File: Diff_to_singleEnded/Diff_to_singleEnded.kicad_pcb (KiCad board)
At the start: 4 copper layers, 85 x 65 mm, 45 parts, among them IC1 ULN2003LVDR, J1 1725672, J2 1725672, J3 1725672, J4 1725672, J5 1725672, J6 1725672, J7 1725672, K3 EE2-5NU, U1 OPA1692xD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

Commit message: removed Relay and power supples related items from board and add seperate ground plains for signal and power
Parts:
- removed C11: 100n, Capacitor_SMD:C_0805_2012Metric_Pad1.18x1.45mm_HandSolder
- removed IC1: ULN2003LVDR, samsys:SOIC127P780X200-16N
- removed J2, J6, J7: 1725672, samsys:1725672
- removed K3: EE2-5NU, samsys:EE2-5NU
- moved J3 13.7 mm to (176.0, 82.3)
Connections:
- C1 pad 2: /Left in -> /Lout
- C13 pad 1: GND -> GND 2
- C14 pad 1: GND -> GND 2
- C15 pad 1: GND -> GND 2
- C2 pad 2: /right in -> /Rout
- J3 pad 1: /right out -> /Lout
- J3 pad 2: GND -> GND 2
- J3 pad 3: GND -> GND 2
- J3 pad 4: /Left Out -> /Rout
- J4 pad 2: GND -> GND 2
- J4 pad 3: GND -> GND 2
- J5 pad 2: GND -> GND 2
- J5 pad 3: GND -> GND 2
- R10 pad 2: /right in -> /Rout
- R5 pad 2: GND -> GND 2
- R6 pad 1: GND -> GND 2
- R8 pad 1: GND -> GND 2
- R9 pad 2: /Left in -> /Lout
- U3 pad 1: /Left in -> /Lout
- U3 pad 7: /right in -> /Rout
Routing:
- net /Lout: track 0.00 -> 47.5 mm, vias 0 -> 1
- net /Rout: track 0.00 -> 42.3 mm, vias 0 -> 1
- net +5VP: track 41.6 -> 0.00 mm, vias 1 -> 0
- net /right in: track 37.9 -> 0.00 mm, vias 1 -> 0
- net /Relay Out: track 34.8 -> 0.00 mm, vias 2 -> 0
- net /Left in: track 33.9 -> 0.00 mm, vias 1 -> 0
- net /right out: track 29.3 -> 0.00 mm
- net /Left Out: track 23.6 -> 0.00 mm
- net /left in ext: track 18.4 -> 0.00 mm
- net /relay 1 in: track 16.4 -> 0.00 mm
- net /right in ext: track 8.18 -> 0.00 mm
- net GND 2: track 0.00 -> 6.68 mm, vias 0 -> 3
- net GND: track 8.83 -> 2.15 mm, vias 137 -> 134
- removed copper zone on B.Cu, net GND
- removed copper zone on F.Cu, net GND
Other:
- board text removed: "5v Relay G"
- board text removed: "G"
- board text removed: "Output"
- board text removed: "Relay"
- board text removed: "Sig"

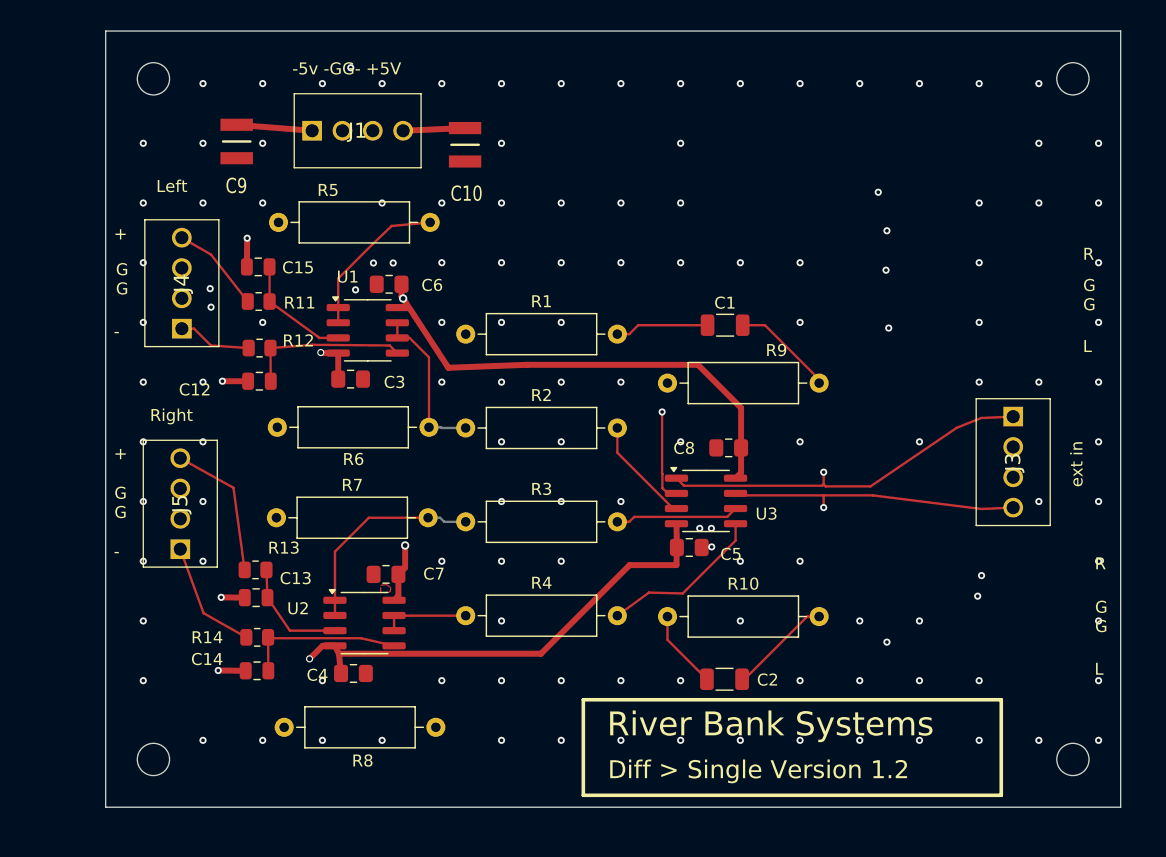
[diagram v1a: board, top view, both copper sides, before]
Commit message: added new rpi power board
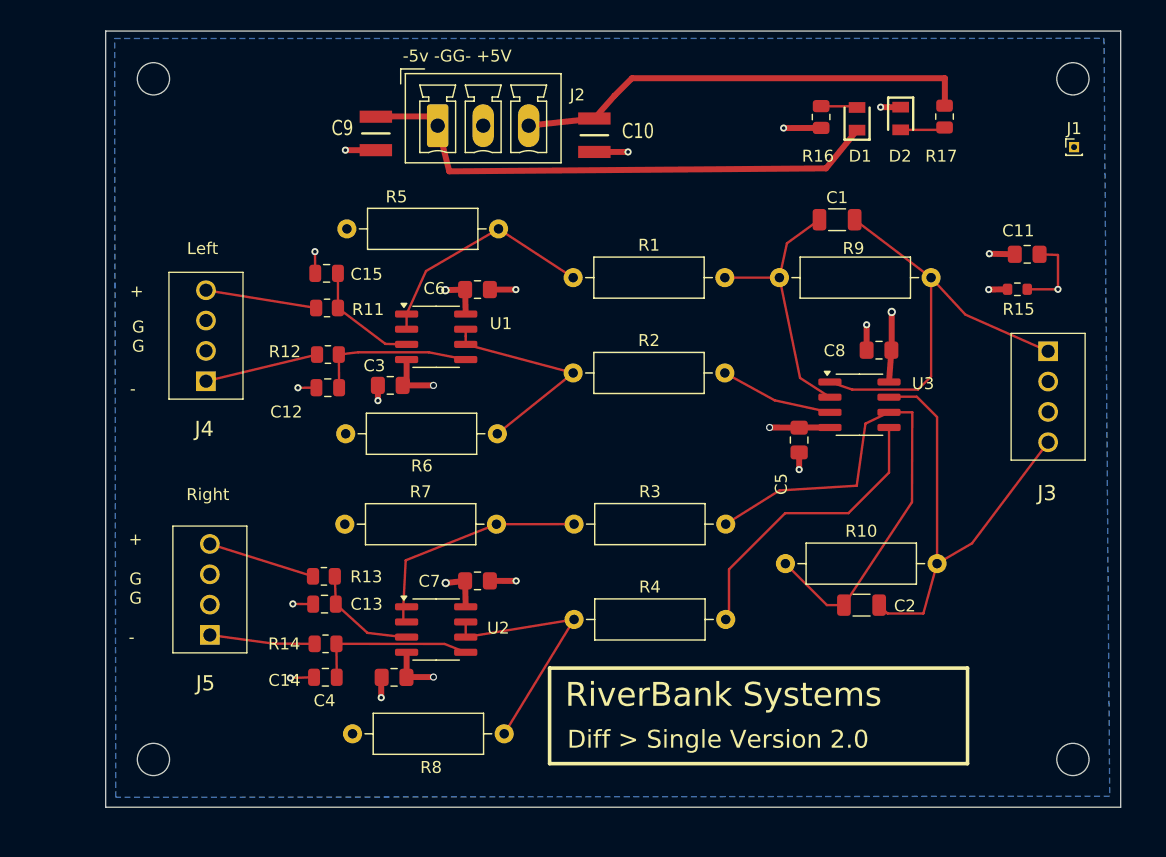
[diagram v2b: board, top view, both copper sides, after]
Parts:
- added C11: 100n, Capacitor_SMD:C_0805_2012Metric_Pad1.18x1.45mm_HandSolder, F.Cu at (177.2, 68.7)
- added D1: LED, samsys:LEDC2012X40N, F.Cu at (162.9, 57.4)
- added D2: LED, samsys:LEDC2012X40N, F.Cu at (166.6, 57.3)
- added J2: Conn_01x03_Socket, Connector_Phoenix_MC:PhoenixContact_MCV_1,5_3-G-3.81_1x03_P3.81mm_Vertical, F.Cu at (127.8, 57.9)
- added R15: 10, Resistor_SMD:R_0603_1608Metric, F.Cu at (176.3, 71.6)
- added R16: 1k, Resistor_SMD:R_0805_2012Metric, F.Cu at (159.9, 57.2)
- added R17: 1k, Resistor_SMD:R_0805_2012Metric, F.Cu at (170.2, 57.2)
- J1: value 1725672 -> Conn_01x01_Pin; footprint samsys:1725672 -> Connector_PinHeader_1.00mm:PinHeader_1x01_P1.00mm_Vertical
- moved J1 63.8 mm to (181.1, 59.7)
- moved U3 15.2 mm to (163.1, 81.3)
- moved C8 15.0 mm to (164.8, 76.7)
- moved C2 13.0 mm to (163.3, 98.1)
- moved C1 12.9 mm to (161.2, 65.8)
- moved R9 12.9 mm to (156.4, 70.7)
- moved C5 12.9 mm to (158.1, 84.2), turned to -90 degrees
- moved C9 11.7 mm to (122.6, 58.6)
- moved C10 10.9 mm to (140.9, 58.7)
- moved R10 10.8 mm to (156.9, 94.6)
- moved R1 10.2 mm to (139.2, 70.7)
- moved R2 10.1 mm to (139.2, 78.6)
- moved R4 9.08 mm to (139.2, 99.3)
- moved R3 9.08 mm to (139.2, 91.3)
- moved C7 7.68 mm to (131.1, 96.0), turned to 180 degrees
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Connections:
- C12 pad 1: GND -> GND 2
- J1 pad 1: -5V -> GND 3
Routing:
- net +5V: track 87.0 -> 160.3 mm, vias 2 -> 3
- net -5V: track 94.7 -> 150.7 mm, vias 2 -> 3
- net GND: track 2.15 -> 24.8 mm, vias 134 -> 12
- net Net-(U3B--): track 26.7 -> 45.8 mm
- net Net-(U3B-+): track 13.8 -> 24.8 mm
- net /Lout: track 47.5 -> 37.1 mm, vias 1 -> 0
- net GND 2: track 6.68 -> 14.0 mm, vias 3 -> 5
- net Net-(U1B--): track 13.6 -> 18.7 mm
- net Net-(U2B--): track 17.7 -> 21.7 mm
- net Net-(U1A--): track 23.6 -> 19.7 mm
- net Net-(D2-A): track 0.00 -> 3.76 mm
- net Net-(J4-Pad1): track 6.19 -> 9.56 mm
- net Net-(D1-A): track 0.00 -> 3.06 mm
- net /Rout: track 42.3 -> 39.3 mm, vias 1 -> 0
- net Net-(J5-Pad4): track 12.0 -> 9.05 mm
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- added copper zone on In3.Cu, net GND
- added copper zone on In1.Cu, net GND 2
- added copper zone on B.Cu, net GND 3
- removed copper zone on F.Cu, net (none)
- removed copper zone on In1.Cu, net GND
- removed copper zone on In2.Cu, net GND
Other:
- copper layers 4 -> 6
- board text added: "Diff > Single Version 2.0"
- board text added: "RiverBank Systems"
- board text removed: "Diff > Single Version 1.2"
- board text removed: "L"
- board text removed: "R"
- board text removed: "River Bank Systems"
- board text removed: "ext in"

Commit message: add updates to se to diff
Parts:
- removed J3, J4, J5: 1725672, samsys:1725672
- added J6: 1725669, samsys:1725669, F.Cu at (106.8, 72.7)
- added J7: 1725669, samsys:1725669, F.Cu at (106.8, 85.1)
- added J8: 1725669, samsys:1725669, F.Cu at (159.9, 82.1)
- moved J1 74.3 mm to (106.8, 60.0)
- moved R16 47.6 mm to (112.4, 54.4)
- moved D1 47.6 mm to (115.4, 54.5)
- moved R8 24.6 mm to (130.2, 86.2), turned to -90 degrees
- moved H4 21.1 mm to (161.5, 103.0)
- moved H3 19.5 mm to (161.5, 53.5)
- moved R17 18.3 mm to (152.2, 54.4)
- moved D2 18.3 mm to (148.5, 54.5)
- moved R15 16.3 mm to (161.0, 66.3)
- moved C11 16.1 mm to (161.1, 68.9)
- moved R9 15.1 mm to (144.4, 79.9), turned to 90 degrees
- moved C2 14.4 mm to (150.3, 91.9), turned to 180 degrees
- moved C1 14.1 mm to (148.8, 72.5)
- moved R10 13.1 mm to (144.5, 98.9), turned to 90 degrees
- moved U3 12.4 mm to (150.8, 81.8)
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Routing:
- net -5V: track 150.7 -> 105.6 mm, vias 3 -> 5
- net +5V: track 160.3 -> 138.3 mm, vias 3 -> 5
- net Net-(U3B--): track 45.8 -> 27.3 mm
- net /Rout: track 39.3 -> 26.4 mm
- net Net-(U1B--): track 18.7 -> 28.9 mm
- net /Lout: track 37.1 -> 27.3 mm
- net Net-(U3B-+): track 24.8 -> 32.9 mm
- net Net-(U2B--): track 21.7 -> 14.1 mm
- net Net-(U2A--): track 19.8 -> 26.9 mm
- net GND: track 24.8 -> 20.5 mm
- net /buffer L- in: track 9.66 -> 6.81 mm
- net GND 2: track 14.0 -> 11.5 mm
- net /buffer L+: track 13.5 -> 11.0 mm
- net /buffer R+ in: track 13.8 -> 11.3 mm
- net /buffer R- in: track 8.93 -> 6.56 mm
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- added copper zone on In2.Cu, net GND
- added copper zone on In4.Cu, net GND 3
- removed copper zone on In3.Cu, net GND
- removed copper zone on B.Cu, net GND 3
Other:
- board size 85 x 65 mm -> 65 x 56.5 mm
- board text added: "-5v -G- +5V"
- board text added: "G"
- board text removed: "-5v -GG- +5V"
- board text removed: "G G"

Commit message: updated final four boards for streamer
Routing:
- net +5V: track 138.3 -> 18.7 mm, vias 5 -> 21
- net -5V: track 105.6 -> 18.6 mm, vias 5 -> 21
- net Net-(U3B--): track 27.3 -> 28.9 mm
- net Net-(U1B--): track 28.9 -> 30.3 mm
- net Net-(U3A--): track 20.1 -> 21.1 mm
- net /Lout: track 27.3 -> 28.0 mm
- net Net-(U3A-+): track 9.00 -> 9.68 mm
- net Net-(U3B-+): track 32.9 -> 33.4 mm
- net GND: vias 12 -> 22
- added copper zone on F.Cu, net (none)
- added copper zone on In2.Cu, net (none)
- added copper zone on F.Cu, net +5V
- added copper zone on In3.Cu, net +5V
- added copper zone on F.Cu, net -5V
- added copper zone on In4.Cu, net -5V
- added copper zone on B.Cu, net GND 3
- removed copper zone on In4.Cu, net GND 3
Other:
- board text added: "Left in"
- board text added: "Left out"
- board text added: "Right in"
- board text added: "Right out"
- board text removed: "Left"
- board text removed: "Right"
